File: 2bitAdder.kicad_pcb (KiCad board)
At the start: 2 copper layers, 53.3 x 71.1 mm, 18 parts, among them J1 Conn_01x02_Male, SW1 SW_Push, SW2 SW_Push, SW3 SW_Push, SW4 SW_Push, U1 74LS386, U2 74LS08, U3 74LS32

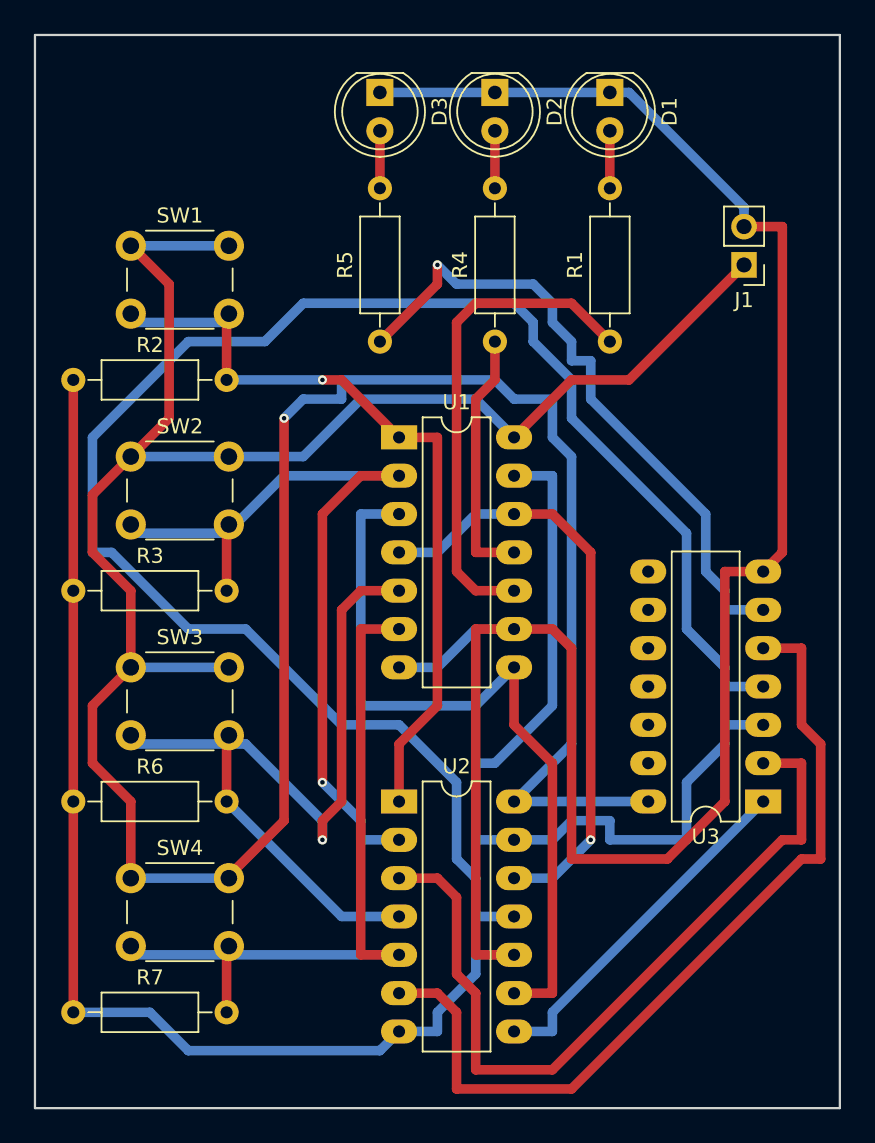
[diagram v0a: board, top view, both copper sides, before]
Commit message: Make vias bigger
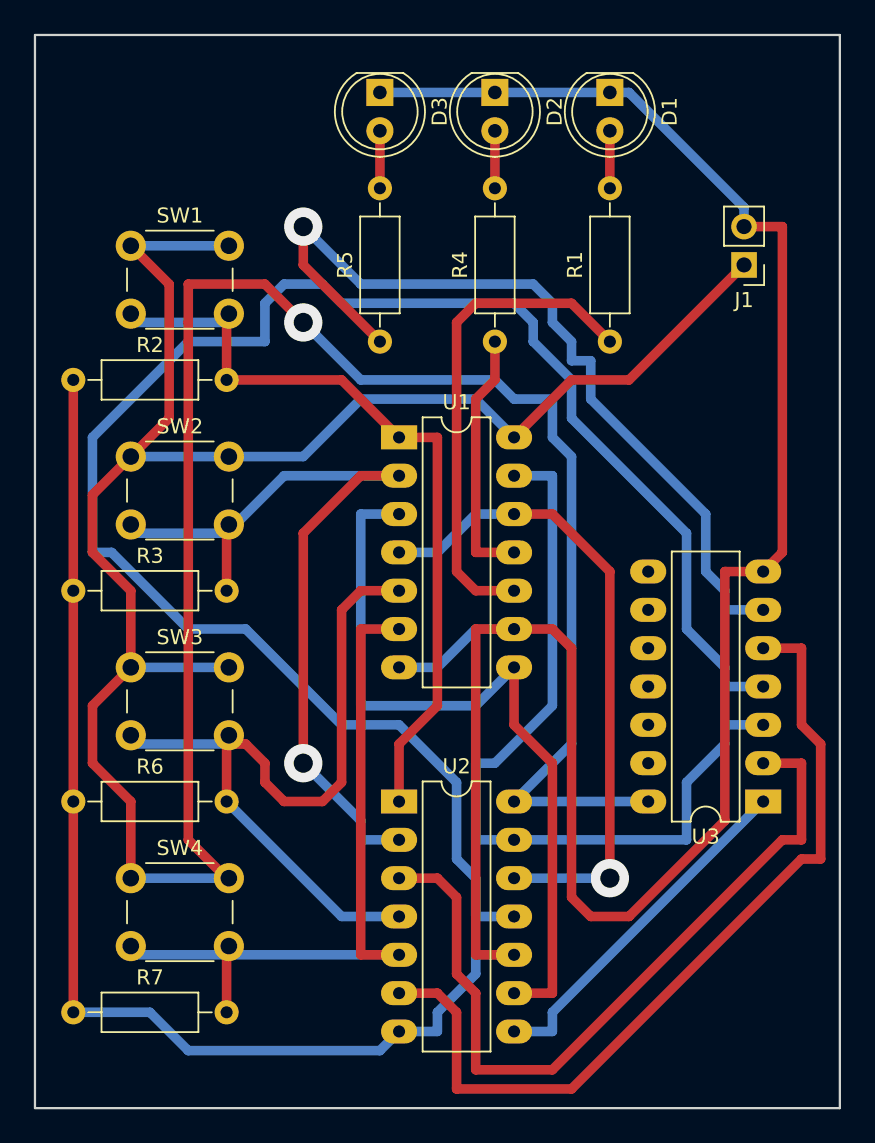
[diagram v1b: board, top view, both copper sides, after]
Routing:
- net VCC: track 205.7 -> 221.2 mm
- net /COUT_1: track 43.7 -> 56.7 mm
- net GND: track 213.9 -> 219.3 mm
- net /A_1: track 56.9 -> 53.4 mm, vias 1 -> 0
- net Net-(U1-Pad12): track 40.0 -> 43.3 mm
- net Net-(U2-Pad11): track 115.4 -> 117.9 mm
- net /COUT_0: track 56.5 -> 54.7 mm
- net /B_0: track 56.9 -> 57.9 mm
- net /A_0: vias 1 -> 0
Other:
- net class Default: via_dia 0.6 -> 2.54; via_drill 0.4 -> 1.5875

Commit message: Add text and board outline
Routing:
- net (no net): track 0.00 -> 497.8 mm
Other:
- board outline removed
- board text added: "2-Bit ADDER"
- board text added: "VECTOR SPACE"
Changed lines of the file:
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@@
     (links 55)
     (no_connects 0)
-    (area 83.82 73.66 140.97 148.59)
+    (area 83.86 74.412499 140.217502 148.55)
     (thickness 1.6)
-    (drawings 5)
-    (tracks 232)
+    (drawings 3)
+    (tracks 240)
     (zones 0)
     (modules 18)
@@
     )
   )
+  (gr_text "VECTOR\nSPACE" (at 95.25 81.28) (layer F.Cu)
+    (effects (font (size 1.5 1.5) (thickness 0.3)))
+  )
+  (gr_text "2-Bit\nADDER" (at 134.62 140.97) (layer F.Cu)
+    (effects (font (size 1.5 1.5) (thickness 0.3)))
+  )
   (target plus (at 86.36 146.05) (size 5) (width 0.15) (layer Edge.Cuts))
-  (gr_line (start 86.36 146.05) (end 86.36 74.93) (angle 90) (layer Edge.Cuts) (width 0.15))
-  (gr_line (start 139.7 146.05) (end 86.36 146.05) (angle 90) (layer Edge.Cuts) (width 0.15))
-  (gr_line (start 139.7 74.93) (end 139.7 146.05) (angle 90) (layer Edge.Cuts) (width 0.15))
-  (gr_line (start 86.36 74.93) (end 139.7 74.93) (angle 90) (layer Edge.Cuts) (width 0.15))
+  (segment (start 86.36 74.93) (end 139.7 74.93) (width 0.635) (layer B.Cu) (net 0))
+  (segment (start 86.36 146.05) (end 86.36 74.93) (width 0.635) (layer B.Cu) (net 0))
+  (segment (start 139.7 146.05) (end 86.36 146.05) (width 0.635) (layer B.Cu) (net 0))
+  (segment (start 139.7 74.93) (end 139.7 146.05) (width 0.635) (layer B.Cu) (net 0))
+  (segment (start 86.36 74.93) (end 139.7 74.93) (width 0.635) (layer F.Cu) (net 0))
+  (segment (start 86.36 146.05) (end 86.36 74.93) (width 0.635) (layer F.Cu) (net 0))
+  (segment (start 139.7 146.05) (end 86.36 146.05) (width 0.635) (layer F.Cu) (net 0))
+  (segment (start 139.7 74.93) (end 139.7 146.05) (width 0.635) (layer F.Cu) (net 0))
   (segment (start 133.35 87.63) (end 133.35 86.36) (width 0.635) (layer B.Cu) (net 1) (status 80000))
   (segment (start 133.35 86.36) (end 125.73 78.74) (width 0.635) (layer B.Cu) (net 1) (status 80000))

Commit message: Add fiducials to help with alignment
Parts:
- added REF**: Fiducial_1mm_Dia_2.54mm_Outer_CopperTop, Fiducials:Fiducial_1mm_Dia_2.54mm_Outer_CopperTop, F.Cu at (135.9, 78.7)
- added REF**: Fiducial_1mm_Dia_2.54mm_Outer_CopperTop, Fiducials:Fiducial_1mm_Dia_2.54mm_Outer_CopperTop, F.Cu at (88.9, 77.5)
- added REF**: Fiducial_1mm_Dia_2.54mm_Outer_CopperTop, Fiducials:Fiducial_1mm_Dia_2.54mm_Outer_CopperTop, F.Cu at (128.3, 143.5)
- added REF**: Fiducial_1mm_Dia_2.54mm_Outer_CopperBottom, Fiducials:Fiducial_1mm_Dia_2.54mm_Outer_CopperBottom, F.Cu at (135.9, 78.7)
- added REF**: Fiducial_1mm_Dia_2.54mm_Outer_CopperBottom, Fiducials:Fiducial_1mm_Dia_2.54mm_Outer_CopperBottom, F.Cu at (88.9, 77.5)
- added REF**: Fiducial_1mm_Dia_2.54mm_Outer_CopperBottom, Fiducials:Fiducial_1mm_Dia_2.54mm_Outer_CopperBottom, F.Cu at (128.3, 143.5)
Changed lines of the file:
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@@
     (links 55)
     (no_connects 0)
-    (area 83.86 74.412499 140.217502 148.55)
+    (area 70.604761 74.412499 154.185239 148.55)
     (thickness 1.6)
     (drawings 3)
     (tracks 240)
     (zones 0)
-    (modules 18)
+    (modules 24)
     (nets 20)
   )
@@
     )
   )
+  (module Fiducials:Fiducial_1mm_Dia_2.54mm_Outer_CopperTop (layer F.Cu)
+    (at 135.89 78.74)
+    (descr "Circular Fiducial, 1mm bare copper top; 2.54mm keepout")
+    (tags marker)
+    (attr virtual)
+    (fp_text reference REF** (at 3.4 0.7) (layer F.SilkS) hide
+      (effects (font (size 1 1) (thickness 0.15)))
+    )
+    (fp_text value Fiducial_1mm_Dia_2.54mm_Outer_CopperTop (at 0 -1.8) (layer F.Fab) hide
+      (effects (font (size 1 1) (thickness 0.15)))
+    )
+    (fp_circle (center 0 0) (end 1.55 0) (layer F.CrtYd) (width 0.05))
+    (pad ~ smd circle (at 0 0) (size 1 1) (layers F.Cu F.Mask)
+      (solder_mask_margin 0.77) (clearance 0.77))
+  )
+  (module Fiducials:Fiducial_1mm_Dia_2.54mm_Outer_CopperTop (layer F.Cu)
+    (at 88.9 77.47)
+    (descr "Circular Fiducial, 1mm bare copper top; 2.54mm keepout")
+    (tags marker)
+    (attr virtual)
+    (fp_text reference REF** (at 3.4 0.7) (layer F.SilkS) hide
+      (effects (font (size 1 1) (thickness 0.15)))
+    )
+    (fp_text value Fiducial_1mm_Dia_2.54mm_Outer_CopperTop (at 0 -1.8) (layer F.Fab) hide
+      (effects (font (size 1 1) (thickness 0.15)))
+    )
+    (fp_circle (center 0 0) (end 1.55 0) (layer F.CrtYd) (width 0.05))
+    (pad ~ smd circle (at 0 0) (size 1 1) (layers F.Cu F.Mask)
+      (solder_mask_margin 0.77) (clearance 0.77))
+  )
+  (module Fiducials:Fiducial_1mm_Dia_2.54mm_Outer_CopperTop (layer F.Cu)
+    (at 128.27 143.51)
+    (descr "Circular Fiducial, 1mm bare copper top; 2.54mm keepout")
+    (tags marker)
+    (attr virtual)
+    (fp_text reference REF** (at 3.4 0.7) (layer F.SilkS) hide
+      (effects (font (size 1 1) (thickness 0.15)))
+    )
+    (fp_text value Fiducial_1mm_Dia_2.54mm_Outer_CopperTop (at 0 -1.8) (layer F.Fab) hide
+      (effects (font (size 1 1) (thickness 0.15)))
+    )
+    (fp_circle (center 0 0) (end 1.55 0) (layer F.CrtYd) (width 0.05))
+    (pad ~ smd circle (at 0 0) (size 1 1) (layers F.Cu F.Mask)
+      (solder_mask_margin 0.77) (clearance 0.77))
+  )
+  (module Fiducials:Fiducial_1mm_Dia_2.54mm_Outer_CopperBottom (layer F.Cu)
+    (at 135.89 78.74)
+    (descr "Circular Fiducial, 1mm bare copper bottom; 2.54mm keepout")
+    (tags marker)
+    (attr virtual)
+    (fp_text reference REF** (at 3.4 0.7) (layer F.SilkS) hide
+      (effects (font (size 1 1) (thickness 0.15)))
+    )
+    (fp_text value Fiducial_1mm_Dia_2.54mm_Outer_CopperBottom (at 0 -1.8) (layer F.Fab) hide
+      (effects (font (size 1 1) (thickness 0.15)))
+    )
+    (fp_circle (center 0 0) (end 1.55 0) (layer B.CrtYd) (width 0.05))
+    (pad ~ smd circle (at 0 0) (size 1 1) (layers B.Cu B.Mask)
+      (solder_mask_margin 0.77) (clearance 0.77))
+  )
+  (module Fiducials:Fiducial_1mm_Dia_2.54mm_Outer_CopperBottom (layer F.Cu)
+    (at 88.9 77.47)
+    (descr "Circular Fiducial, 1mm bare copper bottom; 2.54mm keepout")
+    (tags marker)
+    (attr virtual)
+    (fp_text reference REF** (at 3.4 0.7) (layer F.SilkS) hide
+      (effects (font (size 1 1) (thickness 0.15)))
+    )
+    (fp_text value Fiducial_1mm_Dia_2.54mm_Outer_CopperBottom (at 0 -1.8) (layer F.Fab) hide
+      (effects (font (size 1 1) (thickness 0.15)))
+    )
+    (fp_circle (center 0 0) (end 1.55 0) (layer B.CrtYd) (width 0.05))
+    (pad ~ smd circle (at 0 0) (size 1 1) (layers B.Cu B.Mask)
+      (solder_mask_margin 0.77) (clearance 0.77))
+  )
+  (module Fiducials:Fiducial_1mm_Dia_2.54mm_Outer_CopperBottom (layer F.Cu)
+    (at 128.27 143.51)
+    (descr "Circular Fiducial, 1mm bare copper bottom; 2.54mm keepout")
+    (tags marker)
+    (attr virtual)
+    (fp_text reference REF** (at 3.4 0.7) (layer F.SilkS) hide
+      (effects (font (size 1 1) (thickness 0.15)))
+    )
+    (fp_text value Fiducial_1mm_Dia_2.54mm_Outer_CopperBottom (at 0 -1.8) (layer F.Fab) hide
+      (effects (font (size 1 1) (thickness 0.15)))
+    )
+    (fp_circle (center 0 0) (end 1.55 0) (layer B.CrtYd) (width 0.05))
+    (pad ~ smd circle (at 0 0) (size 1 1) (layers B.Cu B.Mask)
+      (solder_mask_margin 0.77) (clearance 0.77))
+  )
   (gr_text "VECTOR\nSPACE" (at 95.25 81.28) (layer F.Cu)

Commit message: Add board outline to Edge cuts layer
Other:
- board outline added: 53.3 x 71.1 mm
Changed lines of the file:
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@@
     (area 70.604761 74.412499 154.185239 148.55)
     (thickness 1.6)
-    (drawings 3)
+    (drawings 7)
     (tracks 240)
     (zones 0)
@@
       (solder_mask_margin 0.77) (clearance 0.77))
   )
+  (gr_line (start 86.36 146.05) (end 86.36 74.93) (angle 90) (layer Edge.Cuts) (width 0.15))
+  (gr_line (start 139.7 146.05) (end 86.36 146.05) (angle 90) (layer Edge.Cuts) (width 0.15))
+  (gr_line (start 139.7 74.93) (end 139.7 146.05) (angle 90) (layer Edge.Cuts) (width 0.15))
+  (gr_line (start 86.36 74.93) (end 139.7 74.93) (angle 90) (layer Edge.Cuts) (width 0.15))
   (gr_text "VECTOR\nSPACE" (at 95.25 81.28) (layer F.Cu)
     (effects (font (size 1.5 1.5) (thickness 0.3)))

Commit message: Add filled zones
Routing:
- added copper zone on B.Cu, net (none)
- added copper zone on F.Cu, net (none)
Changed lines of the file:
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@@
   (segment (start 137.16 120.65) (end 137.16 115.57) (width 0.635) (layer F.Cu) (net 19) (status 80000))
   (segment (start 137.16 115.57) (end 134.62 115.57) (width 0.635) (layer F.Cu) (net 19) (status 80000))
+  (zone (net 0) (net_name "") (layer F.Cu) (hatch edge 0.508)
+    (connect_pads (clearance 0.508))
+    (min_thickness 0.254)
+    (fill yes (arc_segments 16) (thermal_gap 0.508) (thermal_bridge_width 0.508))
+    (polygon
+      (pts
+        (xy 139.7 146.05) (xy 86.36 146.05) (xy 86.36 74.93) (xy 139.7 74.93)
+      )
+    )
+  )
+  (zone (net 0) (net_name "") (layer B.Cu) (hatch edge 0.508)
+    (connect_pads (clearance 0.508))
+    (min_thickness 0.254)
+    (fill yes (arc_segments 16) (thermal_gap 0.508) (thermal_bridge_width 0.508))
+    (polygon
+      (pts
+        (xy 139.7 146.05) (xy 86.36 146.05) (xy 86.36 74.93) (xy 139.7 74.93)
+      )
+    )
+  )
 )

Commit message: Update netlist
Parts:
- R1, R4, R5: value R -> 220
- R2, R3, R6, R7: value R -> 10K
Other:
- board text added: "2-BIT ADDER"
- board text removed: "2-Bit ADDER"
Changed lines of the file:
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@@
     (links 55)
     (no_connects 0)
-    (area 70.604761 74.412499 154.185239 148.55)
+    (area 86.284999 74.854999 139.775001 146.125001)
     (thickness 1.6)
     (drawings 7)
@@
       (effects (font (size 1 1) (thickness 0.15)))
     )
-    (fp_text value R (at 5.08 2.31 90) (layer F.Fab)
+    (fp_text value 220 (at 5.08 2.31 90) (layer F.Fab)
       (effects (font (size 1 1) (thickness 0.15)))
     )
@@
       (effects (font (size 1 1) (thickness 0.15)))
     )
-    (fp_text value R (at 5.08 2.31) (layer F.Fab)
+    (fp_text value 10K (at 5.08 2.31) (layer F.Fab)
       (effects (font (size 1 1) (thickness 0.15)))
     )
@@
       (effects (font (size 1 1) (thickness 0.15)))
     )
-    (fp_text value R (at 5.08 2.31) (layer F.Fab)
+    (fp_text value 10K (at 5.08 2.31) (layer F.Fab)
       (effects (font (size 1 1) (thickness 0.15)))
     )
@@
       (effects (font (size 1 1) (thickness 0.15)))
     )
-    (fp_text value R (at 5.08 2.31 90) (layer F.Fab)
+    (fp_text value 220 (at 5.08 2.31 90) (layer F.Fab)
       (effects (font (size 1 1) (thickness 0.15)))
     )
@@
       (effects (font (size 1 1) (thickness 0.15)))
     )
-    (fp_text value R (at 5.08 2.31 90) (layer F.Fab)
+    (fp_text value 220 (at 5.08 2.31 90) (layer F.Fab)
       (effects (font (size 1 1) (thickness 0.15)))
     )
@@
       (effects (font (size 1 1) (thickness 0.15)))
     )
-    (fp_text value R (at 5.08 2.31) (layer F.Fab)
+    (fp_text value 10K (at 5.08 2.31) (layer F.Fab)
       (effects (font (size 1 1) (thickness 0.15)))
     )
@@
       (effects (font (size 1 1) (thickness 0.15)))
     )
-    (fp_text value R (at 5.08 2.31) (layer F.Fab)
+    (fp_text value 10K (at 5.08 2.31) (layer F.Fab)
       (effects (font (size 1 1) (thickness 0.15)))
     )
@@
     (effects (font (size 1.5 1.5) (thickness 0.3)))
   )
-  (gr_text "2-Bit\nADDER" (at 134.62 140.97) (layer F.Cu)
+  (gr_text "2-BIT\nADDER" (at 134.62 140.97) (layer F.Cu)
     (effects (font (size 1.5 1.5) (thickness 0.3)))
   )
